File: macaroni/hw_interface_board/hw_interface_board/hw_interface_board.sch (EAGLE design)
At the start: 19 parts, among them M1 455-1750-1-ND, M2 455-1750-1-ND, M3 455-1750-1-ND

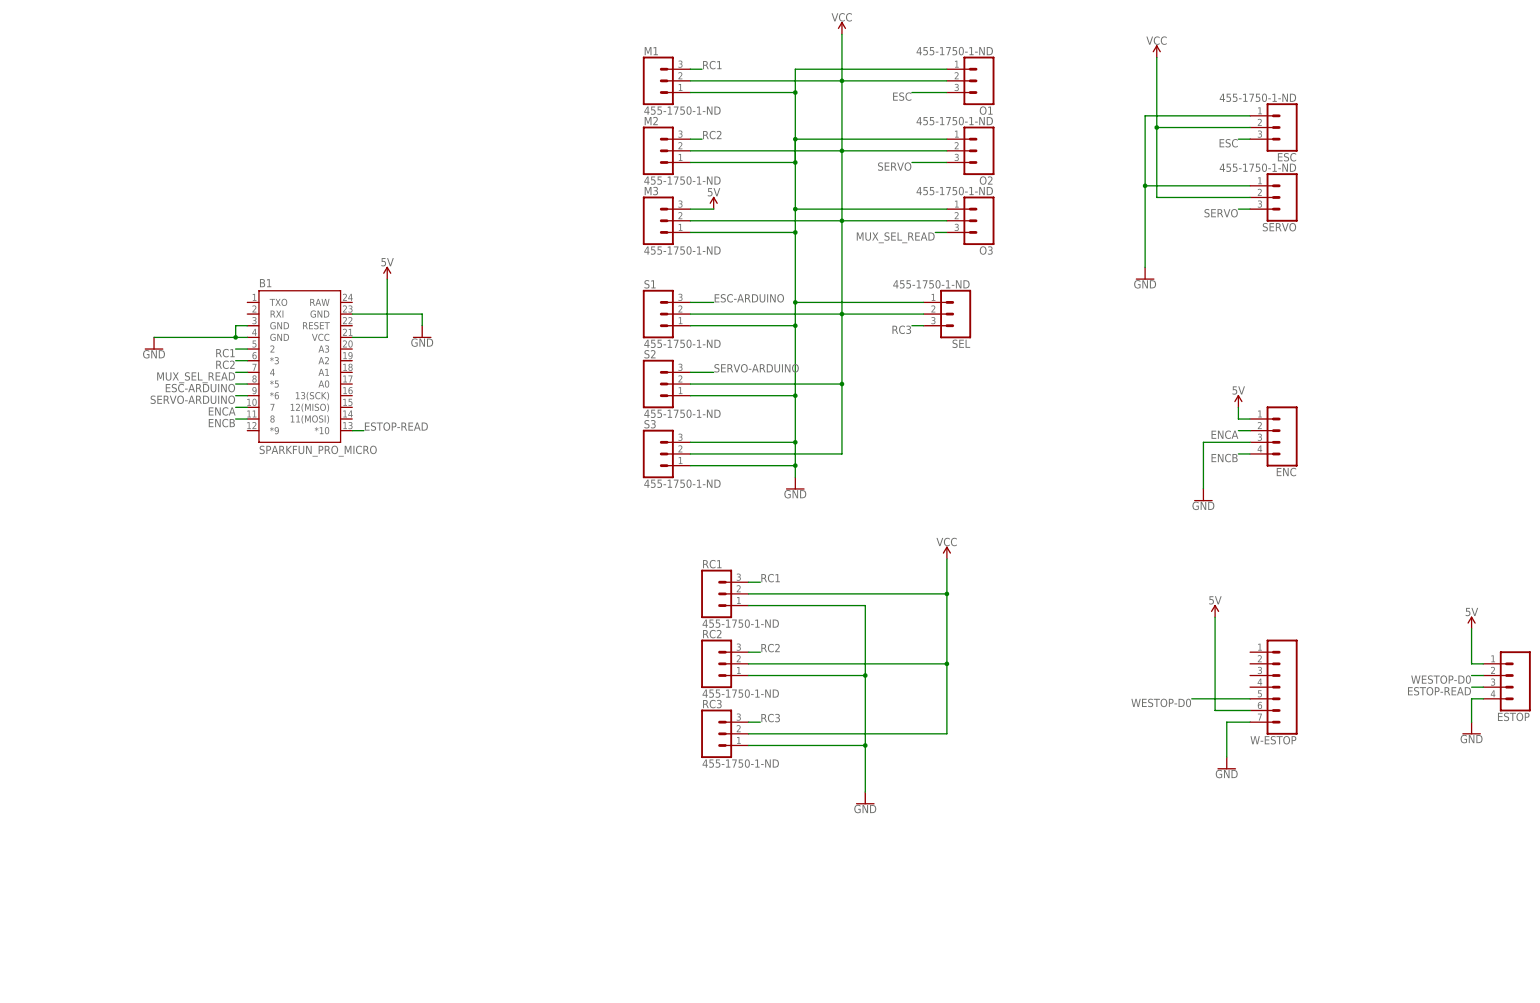
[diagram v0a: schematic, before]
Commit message: Added more functionality to wireless remote, added speaker, fixed pin orientation
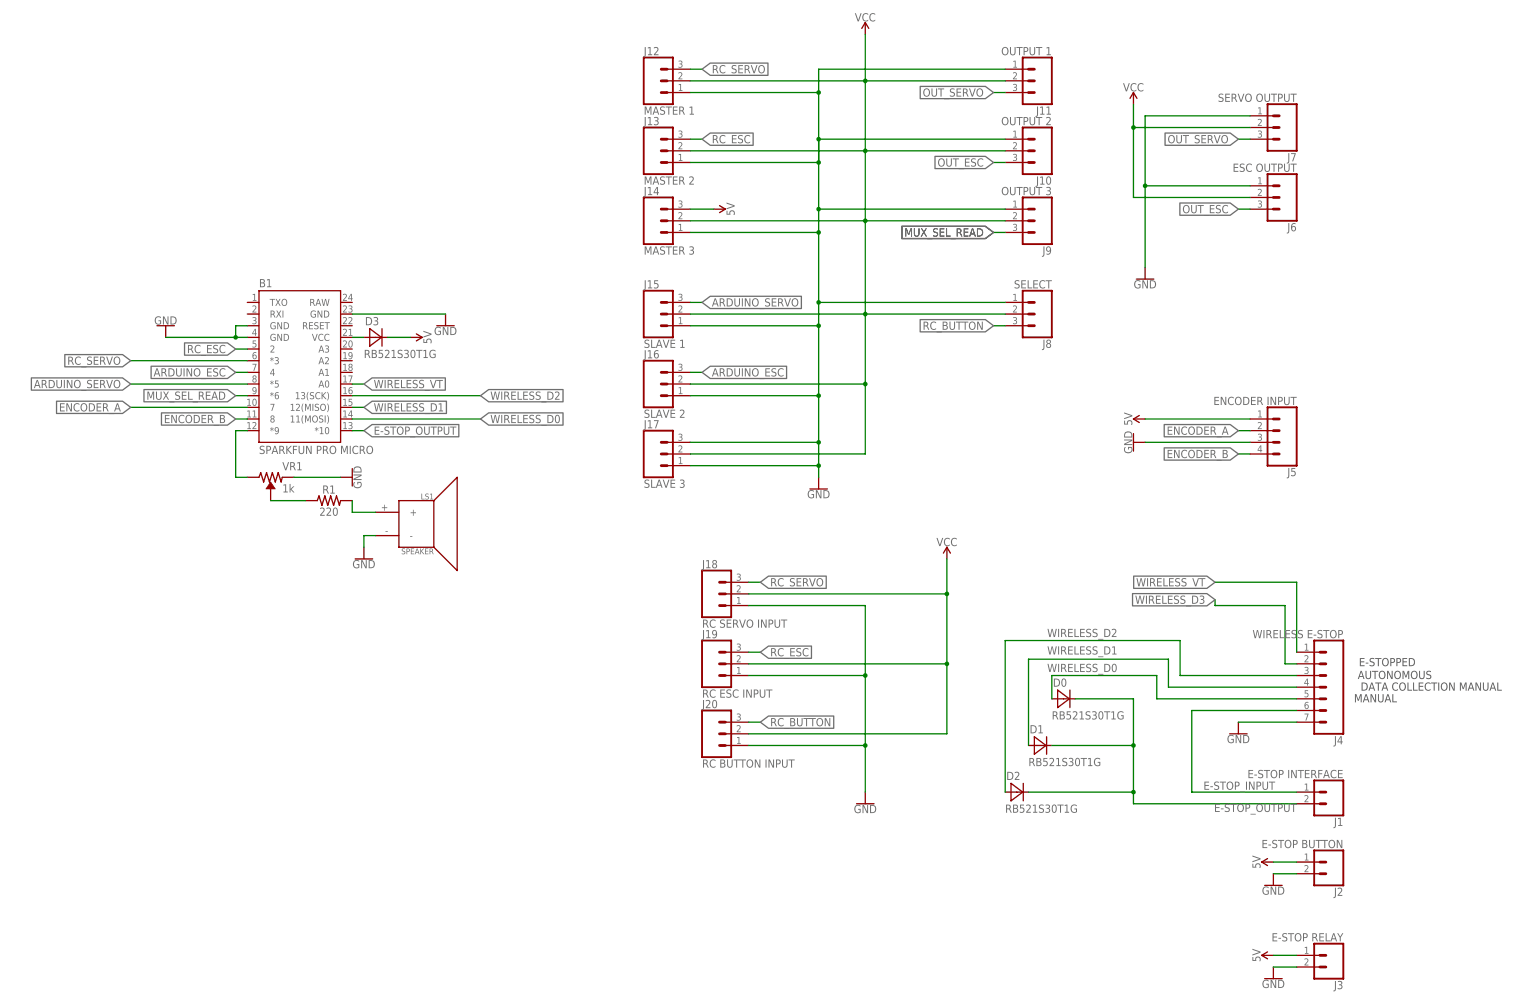
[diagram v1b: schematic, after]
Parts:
- removed ESTOP: (no value), SparkFun-Connectors:CONN_04
- removed O1, O2, O3, SEL: 455-1750-1-ND, SparkFun-Connectors:CONN_03
- removed W-ESTOP: (no value), SparkFun-Connectors:CONN_07
- added D0, D1, D2, D3: RB521S30T1G, mux-board:RB521S30T1G
- added J1: E-STOP INTERFACE, SparkFun-Connectors:CONN_02
- added J10: OUTPUT 2, SparkFun-Connectors:CONN_03
- added J11: OUTPUT 1, SparkFun-Connectors:CONN_03
- added J2: E-STOP BUTTON, SparkFun-Connectors:CONN_02
- added J3: E-STOP RELAY, SparkFun-Connectors:CONN_02
- added J4: WIRELESS E-STOP, SparkFun-Connectors:CONN_07
- added J8: SELECT, SparkFun-Connectors:CONN_03
- added J9: OUTPUT 3, SparkFun-Connectors:CONN_03
- added LS1: SPEAKER, SparkFun-Electromechanical:SPEAKER
- added R1: 220, SparkFun-Resistors:RESISTOR0603
- added VR1: 1k, SparkFun-Resistors:TRIMPOT-PTH-10MM-KNOB-1/2W-10%
- B1: value SPARKFUN_PRO_MICRO -> SPARKFUN PRO MICRO
- J12: value 455-1750-1-ND -> MASTER 1
- J13: value 455-1750-1-ND -> MASTER 2
- J14: value 455-1750-1-ND -> MASTER 3
- J15: value 455-1750-1-ND -> SLAVE 1
- J16: value 455-1750-1-ND -> SLAVE 2
- J17: value 455-1750-1-ND -> SLAVE 3
- J18: value 455-1750-1-ND -> RC SERVO INPUT
- J19: value 455-1750-1-ND -> RC ESC INPUT
- J20: value 455-1750-1-ND -> RC BUTTON INPUT
- J5: value (none) -> ENCODER INPUT
- J6: value 455-1750-1-ND -> ESC OUTPUT
- J7: value 455-1750-1-ND -> SERVO OUTPUT
- renumbered ENC to J5, ESC to J7, M1 to J12, M2 to J13, M3 to J14, RC1 to J18, RC2 to J19, RC3 to J20, S1 to J15, S2 to J16, S3 to J17, SERVO to J6
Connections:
- net ENCA renamed ENCODER_A
- net ENCB renamed ENCODER_B
- net ESC-ARDUINO renamed ARDUINO_SERVO
- removed net ESC: J7.3, O1.3
- removed net ESTOP-READ: B1.*10, ESTOP.3
- removed net RC1: B1.2, J12.3, J18.3
- removed net RC2: B1.*3, J13.3, J19.3
- removed net RC3: J20.3, SEL.3
- removed net SERVO: J6.3, O2.3
- removed net SERVO-ARDUINO: B1.*6, J16.3
- removed net WESTOP-D0: ESTOP.2, W-ESTOP.5
- new net ARDUINO_ESC: B1.4, J16.3
- new net E-STOP_INPUT: J1.1, J4.6
- new net E-STOP_OUTPUT: B1.*10, D0.C, D1.C, D2.C, J1.2
- new net N$1: R1.1, VR1.WIPER
- new net N$2: B1.VCC, D3.A
- new net N$3: LS1.+, R1.2
- new net OUT_ESC: J10.3, J6.3
- new net OUT_SERVO: J11.3, J7.3
- new net RC_BUTTON: J20.3, J8.3
- new net RC_ESC: B1.2, J13.3, J19.3
- new net RC_SERVO: B1.*3, J12.3, J18.3
- new net SPEAKER_OUTPUT: B1.*9, VR1.CW
- new net WIRELESS_D0: B1.11(MOSI), D0.A, J4.5
- new net WIRELESS_D1: B1.12(MISO), D1.A, J4.4
- new net WIRELESS_D2: B1.13(SCK), D2.A, J4.3
- new net WIRELESS_D3: J4.2
- new net WIRELESS_VT: B1.A0, J4.1
- net 5V: now also D3.C, J2.1, J3.1; no longer B1.VCC, ESTOP.1, W-ESTOP.6
- net GND: now also J10.1, J11.1, J2.2, J3.2, J4.7, J8.1, J9.1, LS1.-, VR1.CCW; no longer ESTOP.4, O1.1, O2.1, O3.1, SEL.1, W-ESTOP.7
- net MUX_SEL_READ: now also B1.*6, J9.3; no longer B1.4, O3.3
- net VCC: now also J10.2, J11.2, J8.2, J9.2; no longer O1.2, O2.2, O3.2, SEL.2
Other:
- note added: "AUTONOMOUS"
- note added: "DATA COLLECTION MANUAL"
- note added: "E-STOPPED"
- note added: "MANUAL"

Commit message: Created gerbers for new macaroni control board
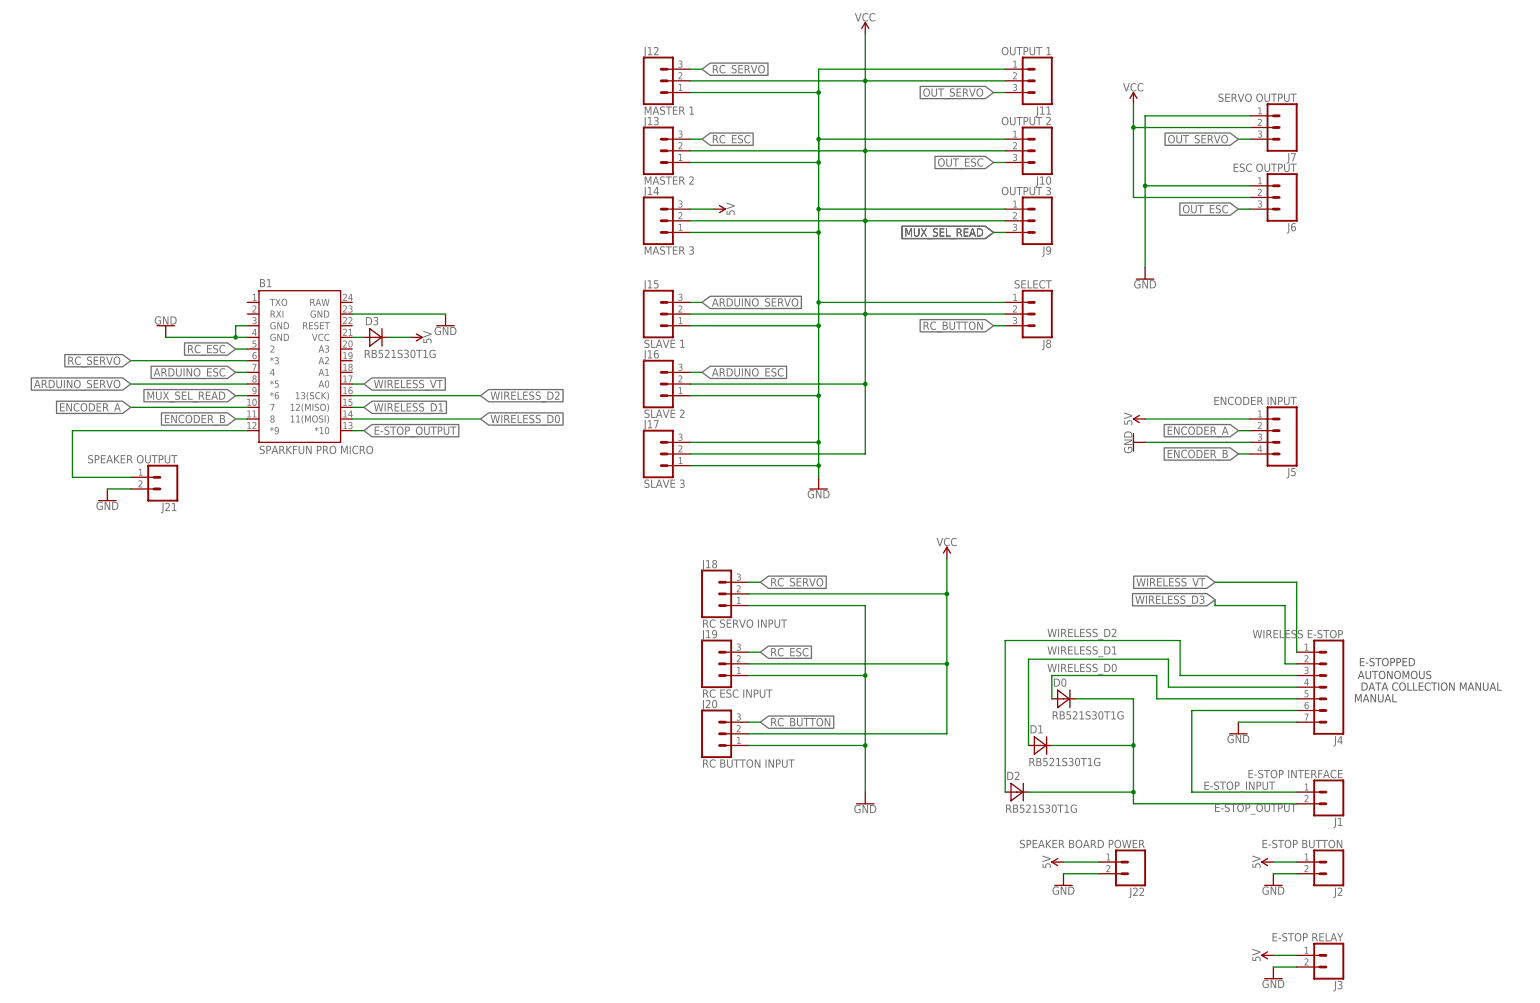
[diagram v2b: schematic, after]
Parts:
- removed LS1: SPEAKER, SparkFun-Electromechanical:SPEAKER
- removed R1: 220, SparkFun-Resistors:RESISTOR0603
- removed VR1: 1k, SparkFun-Resistors:TRIMPOT-PTH-10MM-KNOB-1/2W-10%
- added J21: SPEAKER OUTPUT, SparkFun-Connectors:CONN_02
- added J22: SPEAKER BOARD POWER, SparkFun-Connectors:CONN_02
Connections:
- removed net N$1: R1.1, VR1.WIPER
- removed net N$3: LS1.+, R1.2
- net 5V: now also J22.1
- net GND: now also J21.2, J22.2; no longer LS1.-, VR1.CCW
- net SPEAKER_OUTPUT: now also J21.1; no longer VR1.CW
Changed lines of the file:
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@@
 <?xml version="1.0" encoding="utf-8"?>
 <!DOCTYPE eagle SYSTEM "eagle.dtd">
-<eagle version="8.7.0">
+<eagle version="8.5.0">
 <drawing>
 <settings>
@@
 <part name="D1" library="mux-board" deviceset="RB521S30T1G" device=""/>
 <part name="D0" library="mux-board" deviceset="RB521S30T1G" device=""/>
-<part name="LS1" library="SparkFun-Electromechanical" library_urn="urn:adsk.eagle:library:516" deviceset="SPEAKER" device="" package3d_urn="urn:adsk.eagle:package:38560/1"/>
-<part name="VR1" library="SparkFun-Resistors" library_urn="urn:adsk.eagle:library:532" deviceset="TRIMPOT" device="-PTH-10MM-KNOB-1/2W-10%" package3d_urn="urn:adsk.eagle:package:39662/1" value="1k"/>
-<part name="R1" library="SparkFun-Resistors" library_urn="urn:adsk.eagle:library:532" deviceset="RESISTOR" device="0603" package3d_urn="urn:adsk.eagle:package:39650/1" value="220"/>
+<part name="D3" library="mux-board" deviceset="RB521S30T1G" device=""/>
+<part name="J21" library="SparkFun-Connectors" library_urn="urn:adsk.eagle:library:513" deviceset="CONN_02" device="" package3d_urn="urn:adsk.eagle:package:38039/1" value="SPEAKER OUTPUT"/>
 <part name="GND9" library="SparkFun-PowerSymbols" deviceset="GND" device=""/>
+<part name="J22" library="SparkFun-Connectors" library_urn="urn:adsk.eagle:library:513" deviceset="CONN_02" device="" package3d_urn="urn:adsk.eagle:package:38039/1" value="SPEAKER BOARD POWER"/>
 <part name="GND10" library="SparkFun-PowerSymbols" deviceset="GND" device=""/>
-<part name="D3" library="mux-board" deviceset="RB521S30T1G" device=""/>
+<part name="SUPPLY6" library="SparkFun-PowerSymbols" deviceset="5V" device=""/>
 </parts>
 <sheets>
@@
 <instance part="D1" gate="G$1" x="386.08" y="-17.78"/>
 <instance part="D0" gate="G$1" x="391.16" y="-7.62"/>
-<instance part="LS1" gate="G$1" x="251.46" y="30.48"/>
-<instance part="VR1" gate="R?" x="218.44" y="40.64" rot="R270"/>
-<instance part="R1" gate="G$1" x="231.14" y="35.56"/>
-<instance part="GND9" gate="1" x="238.76" y="22.86"/>
-<instance part="GND10" gate="1" x="236.22" y="40.64" rot="R90"/>
 <instance part="D3" gate="G$1" x="241.3" y="71.12"/>
+<instance part="J21" gate="G$1" x="195.58" y="40.64" rot="R180"/>
+<instance part="GND9" gate="1" x="182.88" y="35.56"/>
+<instance part="J22" gate="G$1" x="406.4" y="-43.18" rot="R180"/>
+<instance part="GND10" gate="1" x="391.16" y="-48.26"/>
+<instance part="SUPPLY6" gate="G$1" x="391.16" y="-43.18" rot="R90"/>
 </instances>
 <busses>
@@
 </segment>
 <segment>
-<pinref part="LS1" gate="G$1" pin="-"/>
-<wire x1="238.76" y1="27.94" x2="238.76" y2="25.4" width="0.1524" layer="91"/>
+<pinref part="J21" gate="G$1" pin="2"/>
+<wire x1="187.96" y1="38.1" x2="182.88" y2="38.1" width="0.1524" layer="91"/>
 <pinref part="GND9" gate="1" pin="GND"/>
-<wire x1="241.3" y1="27.94" x2="238.76" y2="27.94" width="0.1524" layer="91"/>
-</segment>
-<segment>
-<pinref part="VR1" gate="R?" pin="CCW"/>
+</segment>
+<segment>
+<pinref part="J22" gate="G$1" pin="2"/>
+<wire x1="398.78" y1="-45.72" x2="391.16" y2="-45.72" width="0.1524" layer="91"/>
 <pinref part="GND10" gate="1" pin="GND"/>
-<wire x1="223.52" y1="40.64" x2="233.68" y2="40.64" width="0.1524" layer="91"/>
 </segment>
 </net>
@@
 <pinref part="SUPPLY5" gate="G$1" pin="5V"/>
 </segment>
+<segment>
+<pinref part="J22" gate="G$1" pin="1"/>
+<wire x1="398.78" y1="-43.18" x2="391.16" y2="-43.18" width="0.1524" layer="91"/>
+<pinref part="SUPPLY6" gate="G$1" pin="5V"/>
+</segment>
 </net>
 <net name="ENCODER_A" class="0">
@@
 <segment>
 <pinref part="B1" gate="G$1" pin="*9"/>
-<wire x1="213.36" y1="50.8" x2="210.82" y2="50.8" width="0.1524" layer="91"/>
-<wire x1="210.82" y1="50.8" x2="210.82" y2="40.64" width="0.1524" layer="91"/>
-<pinref part="VR1" gate="R?" pin="CW"/>
-<wire x1="210.82" y1="40.64" x2="213.36" y2="40.64" width="0.1524" layer="91"/>
-</segment>
-</net>
-<net name="N$3" class="0">
-<segment>
-<pinref part="R1" gate="G$1" pin="2"/>
-<pinref part="LS1" gate="G$1" pin="+"/>
-<wire x1="241.3" y1="33.02" x2="236.22" y2="33.02" width="0.1524" layer="91"/>
-<wire x1="236.22" y1="35.56" x2="236.22" y2="33.02" width="0.1524" layer="91"/>
-</segment>
-</net>
-<net name="N$1" class="0">
-<segment>
-<pinref part="VR1" gate="R?" pin="WIPER"/>
-<pinref part="R1" gate="G$1" pin="1"/>
-<wire x1="218.44" y1="35.56" x2="226.06" y2="35.56" width="0.1524" layer="91"/>
-</segment>
-</net>
+<wire x1="213.36" y1="50.8" x2="175.26" y2="50.8" width="0.1524" layer="91"/>
+<wire x1="175.26" y1="50.8" x2="175.26" y2="40.64" width="0.1524" layer="91"/>
+<pinref part="J21" gate="G$1" pin="1"/>
+<wire x1="175.26" y1="40.64" x2="187.96" y2="40.64" width="0.1524" layer="91"/>
+</segment>
+</net>
